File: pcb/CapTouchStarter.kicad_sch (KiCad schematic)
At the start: 59 parts, among them J1 USB_C_Receptacle, J2 Conn_ARM_JTAG_SWD_10, J3 62684-50110, Q1 SS8050-G, Q2 SS8050-G, SW1 SW_SPDT, SW2 EN, SW3 BOOT, U1 CP2102N-A01-GQFN28, U2 BD48K33G-TLCT-ND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

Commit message: Switched to KiCAD 6 CP2102N symbol.
It looks like the v5 CP2102N-A01-GQFN28 symbol was renamed
to CP2102N-Axx-xQFN28 in v6.
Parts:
- removed U1: CP2102N-A01-GQFN28, Package_DFN_QFN:QFN-28-1EP_5x5mm_P0.5mm_EP3.35x3.35mm, symbol Interface_USB:CP2102N-A01-GQFN28
- added U1: CP2102N-Axx-xQFN28, Package_DFN_QFN:QFN-28-1EP_5x5mm_P0.5mm_EP3.35x3.35mm, symbol Interface_USB:CP2102N-Axx-xQFN28
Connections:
- net +3V3: now also U1.6 (VDD), U1.7 (VREGIN)
- net D+: now also D1.4 (K), U1.4 (D+); no longer D1.3 (K)
- net D-: now also D1.3 (K), U1.5 (D-); no longer D1.4 (K)
- net DTR: now also U1.28 (~{DTR})
- net GND: now also U1.29 (GND), U1.3 (GND)
- net RTS: now also U1.24 (~{RTS})
- net RXD: now also U1.26 (TXD)
- net TXD: now also U1.25 (RXD)
- net at R3.2: now also U1.9 (~{RST})
- net at R6.1: now also U1.11 (~{SUSPEND})
- net at R1.2, R2.1: now also U1.8 (VBUS)
- net at D3.1 (K): now also U1.19 (~{TXT}/GPIO.0)
- net at D4.1 (K): now also U1.18 (~{RXT}/GPIO.1)
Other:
- moved on the sheet: D1, D3, D4, R1, R2, R6, R7, R8

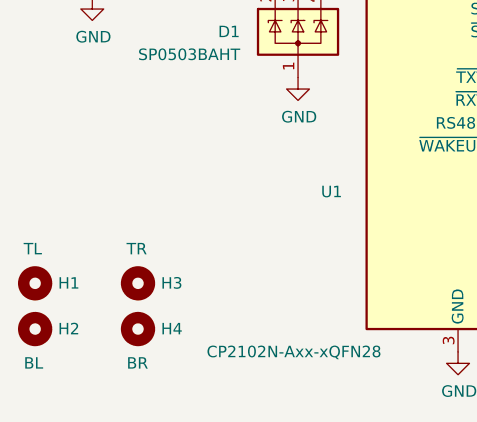
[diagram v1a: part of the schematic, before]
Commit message: Cleanup and IO0 route fix.
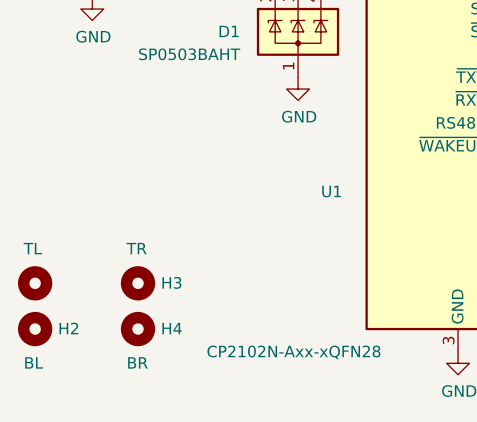
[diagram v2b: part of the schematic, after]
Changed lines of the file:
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@@
     (in_bom yes) (on_board yes)
     (property "Reference" "H1" (id 0) (at 21.59 182.88 0)
-      (effects (font (size 1.27 1.27)) (justify left))
+      (effects (font (size 1.27 1.27)) (justify left) hide)
     )
     (property "Value" "TL" (id 1) (at 17.78 179.07 0)

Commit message: Added PWR_FLAG to help pass ERC.
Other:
- moved on the sheet: TP1
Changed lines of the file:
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@@
   (junction (at 191.77 151.13) (diameter 0) (color 0 0 0 0)
   )
+  (junction (at 93.98 21.59) (diameter 0) (color 0 0 0 0)
+  )
   (junction (at 228.6 27.94) (diameter 0) (color 0 0 0 0)
   )
@@
   )
   (junction (at 207.01 44.45) (diameter 0) (color 0 0 0 0)
+  )
+  (junction (at 29.21 91.44) (diameter 0) (color 0 0 0 0)
+  )
+  (junction (at 138.43 21.59) (diameter 0) (color 0 0 0 0)
   )
   (junction (at 143.51 140.97) (diameter 0) (color 0 0 0 0)
@@
     (stroke (width 0) (type default) (color 0 0 0 0))
   )
+  (wire (pts (xy 29.21 91.44) (xy 38.1 91.44))
+    (stroke (width 0) (type default) (color 0 0 0 0))
+  )
   (wire (pts (xy 105.41 165.1) (xy 105.41 160.02))
     (stroke (width 0) (type default) (color 0 0 0 0))
@@
     (stroke (width 0) (type default) (color 0 0 0 0))
   )
-  (wire (pts (xy 86.36 21.59) (xy 88.9 21.59))
+  (wire (pts (xy 86.36 21.59) (xy 93.98 21.59))
     (stroke (width 0) (type default) (color 0 0 0 0))
   )
@@
     (stroke (width 0) (type default) (color 0 0 0 0))
   )
+  (wire (pts (xy 93.98 19.05) (xy 93.98 21.59))
+    (stroke (width 0) (type default) (color 0 0 0 0))
+  )
   (wire (pts (xy 157.48 66.04) (xy 139.7 66.04))
     (stroke (width 0) (type default) (color 0 0 0 0))
@@
     (stroke (width 0) (type default) (color 0 0 0 0))
   )
+  (wire (pts (xy 93.98 21.59) (xy 93.98 24.13))
+    (stroke (width 0) (type default) (color 0 0 0 0))
+  )
   (wire (pts (xy 35.56 107.95) (xy 30.48 107.95))
     (stroke (width 0) (type default) (color 0 0 0 0))
@@
     (stroke (width 0) (type default) (color 0 0 0 0))
   )
+  (wire (pts (xy 29.21 91.44) (xy 29.21 92.71))
+    (stroke (width 0) (type default) (color 0 0 0 0))
+  )
   (wire (pts (xy 236.22 111.76) (xy 236.22 109.22))
     (stroke (width 0) (type default) (color 0 0 0 0))
@@
     (stroke (width 0) (type default) (color 0 0 0 0))
   )
-  (wire (pts (xy 140.97 21.59) (xy 134.62 21.59))
+  (wire (pts (xy 140.97 21.59) (xy 138.43 21.59))
     (stroke (width 0) (type default) (color 0 0 0 0))
   )
@@
     (stroke (width 0) (type default) (color 0 0 0 0))
   )
+  (wire (pts (xy 29.21 90.17) (xy 29.21 91.44))
+    (stroke (width 0) (type default) (color 0 0 0 0))
+  )
   (wire (pts (xy 238.76 43.18) (xy 238.76 45.72))
     (stroke (width 0) (type default) (color 0 0 0 0))
@@
     (stroke (width 0) (type default) (color 0 0 0 0))
   )
+  (wire (pts (xy 138.43 19.05) (xy 138.43 21.59))
+    (stroke (width 0) (type default) (color 0 0 0 0))
+  )
   (wire (pts (xy 233.68 45.72) (xy 238.76 45.72))
     (stroke (width 0) (type default) (color 0 0 0 0))
@@
   )
   (wire (pts (xy 228.6 19.05) (xy 228.6 27.94))
+    (stroke (width 0) (type default) (color 0 0 0 0))
+  )
+  (wire (pts (xy 138.43 21.59) (xy 134.62 21.59))
     (stroke (width 0) (type default) (color 0 0 0 0))
   )
@@
     (pin "2")
   )
-  (symbol (lib_id "power:GND") (at 29.21 90.17 0) (unit 1)
-    (in_bom yes) (on_board yes)
-    (property "Reference" "#PWR04" (id 0) (at 29.21 96.52 0)
-      (effects (font (size 1.27 1.27)) hide)
-    )
-    (property "Value" "GND" (id 1) (at 29.337 94.5642 0))
-    (property "Footprint" "" (id 2) (at 29.21 90.17 0)
-      (effects (font (size 1.27 1.27)) hide)
-    )
-    (property "Datasheet" "" (id 3) (at 29.21 90.17 0)
+  (symbol (lib_id "power:GND") (at 29.21 92.71 0) (unit 1)
+    (in_bom yes) (on_board yes)
+    (property "Reference" "#PWR04" (id 0) (at 29.21 99.06 0)
+      (effects (font (size 1.27 1.27)) hide)
+    )
+    (property "Value" "GND" (id 1) (at 29.337 97.1042 0))
+    (property "Footprint" "" (id 2) (at 29.21 92.71 0)
+      (effects (font (size 1.27 1.27)) hide)
+    )
+    (property "Datasheet" "" (id 3) (at 29.21 92.71 0)
       (effects (font (size 1.27 1.27)) hide)
     )
@@
     (pin "1")
   )
-  (symbol (lib_id "Connector:TestPoint") (at 88.9 21.59 270) (unit 1)
-    (in_bom yes) (on_board yes)
-    (property "Reference" "TP1" (id 0) (at 93.6752 20.4216 90)
-      (effects (font (size 1.27 1.27)) (justify left))
-    )
-    (property "Value" "5V" (id 1) (at 93.6752 22.733 90)
-      (effects (font (size 1.27 1.27)) (justify left))
-    )
-    (property "Footprint" "TestPoint:TestPoint_Pad_D2.5mm" (id 2) (at 88.9 26.67 0)
-      (effects (font (size 1.27 1.27)) hide)
-    )
-    (property "Datasheet" "~" (id 3) (at 88.9 26.67 0)
+  (symbol (lib_id "Connector:TestPoint") (at 93.98 24.13 180) (unit 1)
+    (in_bom yes) (on_board yes)
+    (property "Reference" "TP1" (id 0) (at 99.06 29.21 0)
+      (effects (font (size 1.27 1.27)) (justify left))
+    )
+    (property "Value" "5V" (id 1) (at 97.79 26.67 0)
+      (effects (font (size 1.27 1.27)) (justify left))
+    )
+    (property "Footprint" "TestPoint:TestPoint_Pad_D2.5mm" (id 2) (at 88.9 24.13 0)
+      (effects (font (size 1.27 1.27)) hide)
+    )
+    (property "Datasheet" "~" (id 3) (at 88.9 24.13 0)
       (effects (font (size 1.27 1.27)) hide)
     )
@@
     (pin "1")
   )
-  (symbol (lib_id "power:VBUS") (at 86.36 19.05 0) (unit 1)
-    (in_bom yes) (on_board yes)
-    (property "Reference" "#PWR013" (id 0) (at 86.36 22.86 0)
-      (effects (font (size 1.27 1.27)) hide)
-    )
-    (property "Value" "VBUS" (id 1) (at 86.741 14.6558 0))
-    (property "Footprint" "" (id 2) (at 86.36 19.05 0)
-      (effects (font (size 1.27 1.27)) hide)
-    )
-    (property "Datasheet" "" (id 3) (at 86.36 19.05 0)
+  (symbol (lib_id "power:VBUS") (at 93.98 19.05 0) (unit 1)
+    (in_bom yes) (on_board yes)
+    (property "Reference" "#PWR013" (id 0) (at 93.98 22.86 0)
+      (effects (font (size 1.27 1.27)) hide)
+    )
+    (property "Value" "VBUS" (id 1) (at 94.361 14.6558 0))
+    (property "Footprint" "" (id 2) (at 93.98 19.05 0)
+      (effects (font (size 1.27 1.27)) hide)
+    )
+    (property "Datasheet" "" (id 3) (at 93.98 19.05 0)
       (effects (font (size 1.27 1.27)) hide)
     )
@@
     (pin "9")
   )
+  (symbol (lib_id "power:PWR_FLAG") (at 138.43 19.05 0) (unit 1)
+    (in_bom yes) (on_board yes) (fields_autoplaced)
+    (property "Reference" "#FLG0103" (id 0) (at 138.43 17.145 0)
+      (effects (font (size 1.27 1.27)) hide)
+    )
+    (property "Value" "PWR_FLAG" (id 1) (at 138.43 13.97 0))
+    (property "Footprint" "" (id 2) (at 138.43 19.05 0)
+      (effects (font (size 1.27 1.27)) hide)
+    )
+    (property "Datasheet" "~" (id 3) (at 138.43 19.05 0)
+      (effects (font (size 1.27 1.27)) hide)
+    )
+    (pin "1")
+  )
   (symbol (lib_id "Interface_USB:CP2102N-Axx-xQFN28") (at 66.04 157.48 0) (unit 1)
     (in_bom yes) (on_board yes)
@@
     (pin "9")
   )
+  (symbol (lib_id "power:PWR_FLAG") (at 38.1 91.44 0) (unit 1)
+    (in_bom yes) (on_board yes) (fields_autoplaced)
+    (property "Reference" "#FLG0102" (id 0) (at 38.1 89.535 0)
+      (effects (font (size 1.27 1.27)) hide)
+    )
+    (property "Value" "PWR_FLAG" (id 1) (at 38.1 86.36 0))
+    (property "Footprint" "" (id 2) (at 38.1 91.44 0)
+      (effects (font (size 1.27 1.27)) hide)
+    )
+    (property "Datasheet" "~" (id 3) (at 38.1 91.44 0)
+      (effects (font (size 1.27 1.27)) hide)
+    )
+    (pin "1")
+  )
+  (symbol (lib_id "power:PWR_FLAG") (at 86.36 19.05 0) (unit 1)
+    (in_bom yes) (on_board yes) (fields_autoplaced)
+    (property "Reference" "#FLG0101" (id 0) (at 86.36 17.145 0)
+      (effects (font (size 1.27 1.27)) hide)
+    )
+    (property "Value" "PWR_FLAG" (id 1) (at 86.36 13.97 0))
+    (property "Footprint" "" (id 2) (at 86.36 19.05 0)
+      (effects (font (size 1.27 1.27)) hide)
+    )
+    (property "Datasheet" "~" (id 3) (at 86.36 19.05 0)
+      (effects (font (size 1.27 1.27)) hide)
+    )
+    (pin "1")
+  )
   (sheet_instances
     (path "/" (page "1"))
   )
   (symbol_instances
+    (path "/f4e92608-53ba-49a5-880c-443776c87820"
+      (reference "#FLG0101") (unit 1) (value "PWR_FLAG") (footprint "")
+    )
+    (path "/df4bd950-daee-4288-94af-8f90ad0d22a3"
+      (reference "#FLG0102") (unit 1) (value "PWR_FLAG") (footprint "")
+    )
+    (path "/a1970094-5545-4754-8eed-12d3fe451497"
+      (reference "#FLG0103") (unit 1) (value "PWR_FLAG") (footprint "")
+    )
     (path "/00000000-0000-0000-0000-0000617a8429"
       (reference "#PWR01") (unit 1) (value "GND") (footprint "")

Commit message: Add JTAG RESET series resistor.
Eliminate the following ERC warning:

    "Pins of type Output and Open collector are connector".

Discussion at
https://www.reddit.com/r/AskElectronics/comments/754epz/series_resistors_on_jtag_lines/

Also, fixed D+/D- ESD pad assignments and a few silkscreen inside
cut boundaries ERC warnings.
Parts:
- added R20: 39Ω, Resistor_SMD:R_0603_1608Metric, symbol Device:R_Small
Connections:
- net EN: now also R20.2; no longer J2.10 (~{RESET})
- new net: J2.10 (~{RESET}), R20.1
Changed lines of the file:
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@@
     )
   )
-  (global_label "EN" (shape input) (at 113.03 68.58 0) (fields_autoplaced)
-    (effects (font (size 1.27 1.27)) (justify left))
-    (property "Intersheet References" "${INTERSHEET_REFS}" (id 0) (at 0 0 0)
+  (global_label "EN" (shape input) (at 118.11 68.58 0) (fields_autoplaced)
+    (effects (font (size 1.27 1.27)) (justify left))
+    (property "Intersheet References" "${INTERSHEET_REFS}" (id 0) (at 5.08 0 0)
       (effects (font (size 1.27 1.27)) hide)
     )
@@
     (pin "9")
   )
+  (symbol (lib_id "Device:R_Small") (at 115.57 68.58 90) (unit 1)
+    (in_bom yes) (on_board yes)
+    (property "Reference" "R20" (id 0) (at 116.84 63.5 90)
+      (effects (font (size 1.27 1.27)) (justify left))
+    )
+    (property "Value" "39Ω" (id 1) (at 118.11 66.04 90)
+      (effects (font (size 1.27 1.27)) (justify left))
+    )
+    (property "Footprint" "Resistor_SMD:R_0603_1608Metric" (id 2) (at 115.57 68.58 0)
+      (effects (font (size 1.27 1.27)) hide)
+    )
+    (property "Datasheet" "~" (id 3) (at 115.57 68.58 0)
+      (effects (font (size 1.27 1.27)) hide)
+    )
+    (pin "1")
+    (pin "2")
+  )
   (symbol (lib_id "power:PWR_FLAG") (at 138.43 19.05 0) (unit 1)
     (in_bom yes) (on_board yes) (fields_autoplaced)
@@
       (reference "R19") (unit 1) (value "68Ω") (footprint "Resistor_SMD:R_0603_1608Metric")
     )
+    (path "/4f59afea-52a6-42ef-a827-b3f6d4652563"
+      (reference "R20") (unit 1) (value "39Ω") (footprint "Resistor_SMD:R_0603_1608Metric")
+    )
     (path "/00000000-0000-0000-0000-00006189a8b9"

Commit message: Switch to cmumford-components for KiCad components.
https://github.com/cmumford/cmumford-components.git
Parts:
- J3: footprint 0541325062:0541325062 -> cmumford-footprints:62684-50110; symbol 62684-50110:62684-50110 -> cmumford-symbols:62684-50110
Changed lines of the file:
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@@
     )
   )
-  (symbol (lib_id "62684-50110:62684-50110") (at 254 86.36 0) (mirror x) (unit 1)
+  (symbol (lib_id "cmumford-symbols:62684-50110") (at 254 86.36 0) (mirror x) (unit 1)
     (in_bom yes) (on_board yes)
     (property "Reference" "J3" (id 0) (at 262.382 86.2584 0)
@@
       (effects (font (size 1.27 1.27)) (justify left))
     )
-    (property "Footprint" "0541325062:0541325062" (id 2) (at 264.16 90.17 0)
+    (property "Footprint" "cmumford-footprints:62684-50110" (id 2) (at 264.16 90.17 0)
       (effects (font (size 1.27 1.27)) (justify left bottom) hide)
     )
-    (property "Datasheet" "" (id 3) (at 254 86.36 0)
+    (property "Datasheet" "https://cdn-shop.adafruit.com/datasheets/62684.pdf" (id 3) (at 254 86.36 0)
       (effects (font (size 1.27 1.27)) (justify left bottom) hide)
     )
@@
     )
     (path "/00000000-0000-0000-0000-00006133b4ee"
-      (reference "J3") (unit 1) (value "62684-50110") (footprint "0541325062:0541325062")
+      (reference "J3") (unit 1) (value "62684-50110") (footprint "cmumford-symbols:62684-50110")
     )
     (path "/00000000-0000-0000-0000-0000617c491d"

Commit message: Added network labels.
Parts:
- J3: footprint cmumford-footprints:62684-50110 -> cmumford-symbols:62684-50110
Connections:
- net EN: now also J2.10 (~{RESET}), R20.1
- net VBUS: now also D2.1 (K), D2.2 (A), J1.A4 (VBUS), J1.A9 (VBUS), J1.B4 (VBUS), J1.B9 (VBUS), R1.2, R2.1, SW1.2 (B), U1.8 (VBUS)
- net CC1: now reaches J1.A5 (CC1), R4.1
- net CC2: now reaches J1.B5 (CC2), R5.1
- net RST: now reaches R3.2, U1.9 (~{RST})
- net SUSPEND: now reaches R6.1, U1.11 (~{SUSPEND})
- net TX: now reaches D3.1 (K), U1.19 (~{TXT}/GPIO.0)
- net RX: now reaches D4.1 (K), U1.18 (~{RXT}/GPIO.1)
- net UTIL_LED: now reaches R11.1, U3.8 (IO32)
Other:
- moved on the sheet: D2, R20, R6
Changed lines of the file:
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@@
     (stroke (width 0) (type default) (color 0 0 0 0))
   )
-  (wire (pts (xy 44.45 24.13) (xy 46.99 24.13))
+  (wire (pts (xy 44.45 24.13) (xy 52.07 24.13))
     (stroke (width 0) (type default) (color 0 0 0 0))
   )
@@
     (stroke (width 0) (type default) (color 0 0 0 0))
   )
+  (wire (pts (xy 59.69 24.13) (xy 72.39 24.13))
+    (stroke (width 0) (type default) (color 0 0 0 0))
+  )
   (wire (pts (xy 30.48 116.84) (xy 30.48 119.38))
     (stroke (width 0) (type default) (color 0 0 0 0))
@@
     (stroke (width 0) (type default) (color 0 0 0 0))
   )
+  (wire (pts (xy 113.03 68.58) (xy 119.38 68.58))
+    (stroke (width 0) (type default) (color 0 0 0 0))
+  )
+  (wire (pts (xy 82.55 147.32) (xy 91.44 147.32))
+    (stroke (width 0) (type default) (color 0 0 0 0))
+  )
   (wire (pts (xy 130.81 135.89) (xy 128.27 135.89))
     (stroke (width 0) (type default) (color 0 0 0 0))
@@
     (stroke (width 0) (type default) (color 0 0 0 0))
   )
-  (wire (pts (xy 54.61 24.13) (xy 72.39 24.13))
-    (stroke (width 0) (type default) (color 0 0 0 0))
-  )
   (wire (pts (xy 238.76 127) (xy 238.76 129.54))
     (stroke (width 0) (type default) (color 0 0 0 0))
@@
     (stroke (width 0) (type default) (color 0 0 0 0))
   )
-  (wire (pts (xy 92.71 147.32) (xy 93.98 147.32))
+  (wire (pts (xy 99.06 147.32) (xy 100.33 147.32))
     (stroke (width 0) (type default) (color 0 0 0 0))
   )
@@
   )
   (wire (pts (xy 240.03 152.4) (xy 240.03 139.7))
-    (stroke (width 0) (type default) (color 0 0 0 0))
-  )
-  (wire (pts (xy 85.09 147.32) (xy 82.55 147.32))
     (stroke (width 0) (type default) (color 0 0 0 0))
   )
@@
     (effects (font (size 1.27 1.27)) (justify left bottom))
   )
+  (label "EN" (at 114.3 68.58 0)
+    (effects (font (size 1.27 1.27)) (justify left bottom))
+  )
+  (label "VBUS" (at 46.99 142.24 0)
+    (effects (font (size 1.27 1.27)) (justify left bottom))
+  )
+  (label "VBUS" (at 63.5 24.13 0)
+    (effects (font (size 1.27 1.27)) (justify left bottom))
+  )
+  (label "CC1" (at 46.99 29.21 0)
+    (effects (font (size 1.27 1.27)) (justify left bottom))
+  )
+  (label "UTIL_LED" (at 144.78 66.04 0)
+    (effects (font (size 1.27 1.27)) (justify left bottom))
+  )
+  (label "SUSPEND" (at 82.55 147.32 0)
+    (effects (font (size 1.27 1.27)) (justify left bottom))
+  )
+  (label "TX" (at 80.01 160.02 0)
+    (effects (font (size 1.27 1.27)) (justify left bottom))
+  )
+  (label "CC2" (at 46.99 31.75 0)
+    (effects (font (size 1.27 1.27)) (justify left bottom))
+  )
+  (label "RST" (at 49.53 129.54 0)
+    (effects (font (size 1.27 1.27)) (justify left bottom))
+  )
+  (label "VBUS" (at 45.72 24.13 0)
+    (effects (font (size 1.27 1.27)) (justify left bottom))
+  )
+  (label "RX" (at 80.01 162.56 0)
+    (effects (font (size 1.27 1.27)) (justify left bottom))
+  )
   (global_label "TXD" (shape input) (at 78.74 132.08 0) (fields_autoplaced)
     (effects (font (size 1.27 1.27)) (justify left))
@@
     )
   )
-  (global_label "EN" (shape input) (at 118.11 68.58 0) (fields_autoplaced)
+  (global_label "EN" (shape input) (at 124.46 68.58 0) (fields_autoplaced)
     (effects (font (size 1.27 1.27)) (justify left))
-    (property "Intersheet References" "${INTERSHEET_REFS}" (id 0) (at 5.08 0 0)
+    (property "Intersheet References" "${INTERSHEET_REFS}" (id 0) (at 11.43 0 0)
       (effects (font (size 1.27 1.27)) hide)
     )
@@
       (effects (font (size 1.27 1.27)) (justify left))
     )
-    (property "Footprint" "cmumford-footprints:62684-50110" (id 2) (at 264.16 90.17 0)
+    (property "Footprint" "cmumford-symbols:62684-50110" (id 2) (at 264.16 90.17 0)
       (effects (font (size 1.27 1.27)) (justify left bottom) hide)
     )
@@
     (pin "S1")
   )
-  (symbol (lib_id "Device:D_Schottky") (at 50.8 24.13 180) (unit 1)
-    (in_bom yes) (on_board yes)
-    (property "Reference" "D2" (id 0) (at 50.8 18.6182 0))
-    (property "Value" "BAT760-7" (id 1) (at 50.8 20.9296 0))
-    (property "Footprint" "Diode_SMD:D_SOD-323" (id 2) (at 50.8 24.13 0)
-      (effects (font (size 1.27 1.27)) hide)
-    )
-    (property "Datasheet" "~" (id 3) (at 50.8 24.13 0)
+  (symbol (lib_id "Device:D_Schottky") (at 55.88 24.13 180) (unit 1)
+    (in_bom yes) (on_board yes)
+    (property "Reference" "D2" (id 0) (at 55.88 18.6182 0))
+    (property "Value" "BAT760-7" (id 1) (at 55.88 20.9296 0))
+    (property "Footprint" "Diode_SMD:D_SOD-323" (id 2) (at 55.88 24.13 0)
+      (effects (font (size 1.27 1.27)) hide)
+    )
+    (property "Datasheet" "~" (id 3) (at 55.88 24.13 0)
       (effects (font (size 1.27 1.27)) hide)
     )
@@
     (pin "1")
   )
-  (symbol (lib_id "Device:R") (at 88.9 147.32 90) (unit 1)
-    (in_bom yes) (on_board yes)
-    (property "Reference" "R6" (id 0) (at 90.17 144.78 90)
-      (effects (font (size 1.27 1.27)) (justify left))
-    )
-    (property "Value" "10KΩ" (id 1) (at 91.44 149.86 90)
-      (effects (font (size 1.27 1.27)) (justify left))
-    )
-    (property "Footprint" "Resistor_SMD:R_0603_1608Metric" (id 2) (at 88.9 149.098 90)
-      (effects (font (size 1.27 1.27)) hide)
-    )
-    (property "Datasheet" "~" (id 3) (at 88.9 147.32 0)
-      (effects (font (size 1.27 1.27)) hide)
-    )
-    (pin "1")
-    (pin "2")
-  )
-  (symbol (lib_id "power:GND") (at 93.98 147.32 0) (unit 1)
-    (in_bom yes) (on_board yes)
-    (property "Reference" "#PWR012" (id 0) (at 93.98 153.67 0)
-      (effects (font (size 1.27 1.27)) hide)
-    )
-    (property "Value" "GND" (id 1) (at 94.107 151.7142 0))
-    (property "Footprint" "" (id 2) (at 93.98 147.32 0)
-      (effects (font (size 1.27 1.27)) hide)
-    )
-    (property "Datasheet" "" (id 3) (at 93.98 147.32 0)
+  (symbol (lib_id "Device:R") (at 95.25 147.32 90) (unit 1)
+    (in_bom yes) (on_board yes)
+    (property "Reference" "R6" (id 0) (at 96.52 144.78 90)
+      (effects (font (size 1.27 1.27)) (justify left))
+    )
+    (property "Value" "10KΩ" (id 1) (at 97.79 149.86 90)
+      (effects (font (size 1.27 1.27)) (justify left))
+    )
+    (property "Footprint" "Resistor_SMD:R_0603_1608Metric" (id 2) (at 95.25 149.098 90)
+      (effects (font (size 1.27 1.27)) hide)
+    )
+    (property "Datasheet" "~" (id 3) (at 95.25 147.32 0)
+      (effects (font (size 1.27 1.27)) hide)
+    )
+    (pin "1")
+    (pin "2")
+  )
+  (symbol (lib_id "power:GND") (at 100.33 147.32 0) (unit 1)
+    (in_bom yes) (on_board yes)
+    (property "Reference" "#PWR012" (id 0) (at 100.33 153.67 0)
+      (effects (font (size 1.27 1.27)) hide)
+    )
+    (property "Value" "GND" (id 1) (at 100.457 151.7142 0))
+    (property "Footprint" "" (id 2) (at 100.33 147.32 0)
+      (effects (font (size 1.27 1.27)) hide)
+    )
+    (property "Datasheet" "" (id 3) (at 100.33 147.32 0)
       (effects (font (size 1.27 1.27)) hide)
     )
@@
     (pin "9")
   )
-  (symbol (lib_id "Device:R_Small") (at 115.57 68.58 90) (unit 1)
-    (in_bom yes) (on_board yes)
-    (property "Reference" "R20" (id 0) (at 116.84 63.5 90)
-      (effects (font (size 1.27 1.27)) (justify left))
-    )
-    (property "Value" "39Ω" (id 1) (at 118.11 66.04 90)
-      (effects (font (size 1.27 1.27)) (justify left))
-    )
-    (property "Footprint" "Resistor_SMD:R_0603_1608Metric" (id 2) (at 115.57 68.58 0)
-      (effects (font (size 1.27 1.27)) hide)
-    )
-    (property "Datasheet" "~" (id 3) (at 115.57 68.58 0)
-      (effects (font (size 1.27 1.27)) hide)
-    )
+  (symbol (lib_id "Device:R_Small") (at 121.92 68.58 90) (unit 1)
+    (in_bom yes) (on_board yes)
+    (property "Reference" "R20" (id 0) (at 123.19 63.5 90)
+      (effects (font (size 1.27 1.27)) (justify left))
+    )
+    (property "Value" "39Ω" (id 1) (at 124.46 66.04 90)
+      (effects (font (size 1.27 1.27)) (justify left))
+    )
+    (property "Footprint" "Resistor_SMD:R_0603_1608Metric" (id 2) (at 121.92 68.58 0)
+      (effects (font (size 1.27 1.27)) hide)
+    )
+    (property "Datasheet" "~" (id 3) (at 121.92 68.58 0)
+      (effects (font (size 1.27 1.27)) hide)
+    )
